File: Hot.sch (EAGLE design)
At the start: 21 parts, among them Q1 BC817, T1 BTA24-600

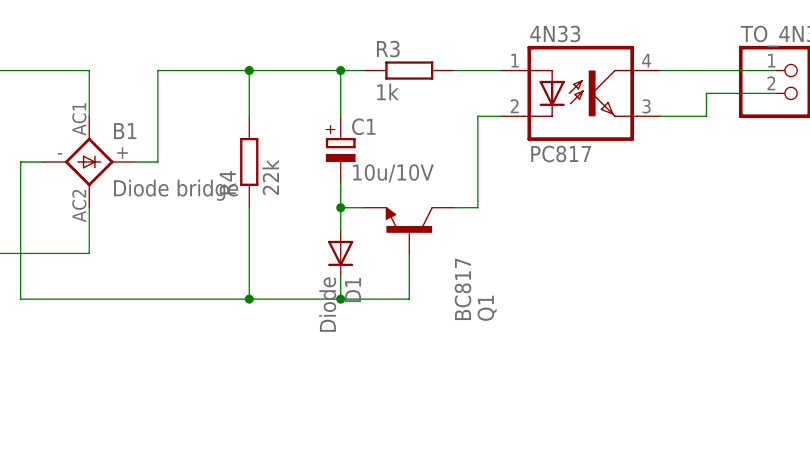
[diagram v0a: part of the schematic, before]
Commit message: Переразвел 2горячую" плату - уменьшил длинну упарвляющей дорожки, увеличил ширину силовых дорожек. Под тиристором уменьшились зазоры - на перетрав, при необходимости - доработать напильником %) Добавил подписи "+" на разъемах
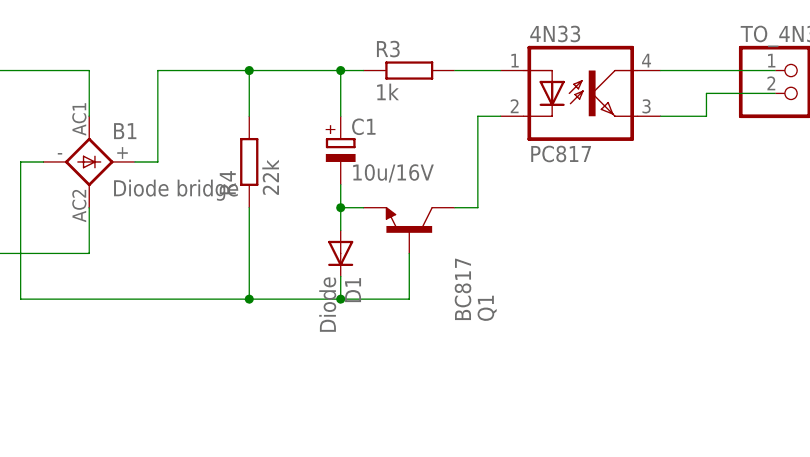
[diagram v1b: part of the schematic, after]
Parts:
- C1: value 10u/10V -> 10u/16V
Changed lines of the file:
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@@
 <part name="R3" library="rcl" deviceset="R-EU_" device="M1206" value="1k"/>
 <part name="R4" library="rcl" deviceset="R-EU_" device="M1206" value="22k"/>
-<part name="C1" library="rcl" deviceset="CPOL-EU" device="E2.5-5" value="10u/10V"/>
+<part name="C1" library="rcl" deviceset="CPOL-EU" device="E2.5-5" value="10u/16V"/>
 <part name="Q1" library="transistor-npn" deviceset="BC817*" device="SMD" technology="-16LT1" value="BC817"/>
 <part name="L" library="solpad" deviceset="LSP10" device=""/>
